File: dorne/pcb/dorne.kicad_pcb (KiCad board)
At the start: 2 copper layers, 275.5 x 105.6 mm, 92 parts, among them J1 MJ-4PP-9, J2 OLED, J3 MJ-4PP-9, J4 OLED, SW1 SW_PUSH, SW10 SW_PUSH, SW11 SW_PUSH, SW12 SW_PUSH, SW13 SW_PUSH, SW14 SW_PUSH, SW15 SW_PUSH, SW16 SW_PUSH, SW17 SW_PUSH, SW18 SW_PUSH, SW19 SW_PUSH, SW2 SW_PUSH, SW20 SW_PUSH, SW21 SW_PUSH, SW22 SW_PUSH, SW23 SW_PUSH, SW24 SW_PUSH, SW25 SW_PUSH, SW26 SW_PUSH, SW27 SW_PUSH, SW28 SW_PUSH, SW29 SW_PUSH, SW3 SW_PUSH, SW30 SW_PUSH, SW31 SW_PUSH, SW32 SW_PUSH, SW33 SW_PUSH, SW34 SW_PUSH, SW35 SW_PUSH, SW36 SW_PUSH, SW37 SW_PUSH, SW38 SW_PUSH, SW39 SW_PUSH, SW4 SW_PUSH, SW40 SW_PUSH, SW41 SW_PUSH, SW42 SW_PUSH, SW5 SW_PUSH, SW6 SW_PUSH, SW7 SW_PUSH, SW8 SW_PUSH, SW9 SW_PUSH, U1 ProMicro, U2 ProMicro

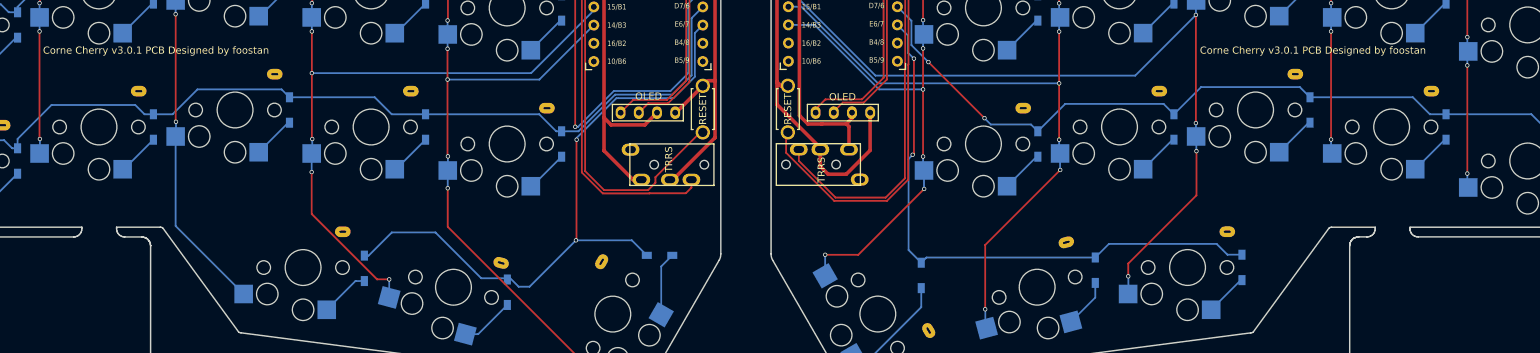
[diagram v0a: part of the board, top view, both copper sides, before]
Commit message: Fix Diode issue
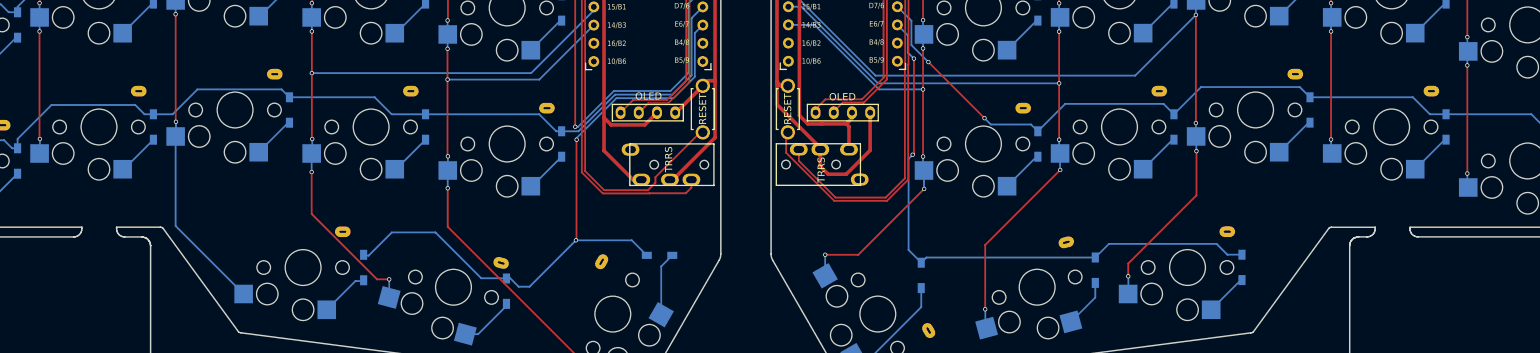
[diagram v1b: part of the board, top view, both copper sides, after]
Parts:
- U3: renamed from U1; value ProMicro -> NiceNano
- moved D19 20.4 mm to (95.1, 88.7)
- moved D20 20.1 mm to (115.0, 92.0)
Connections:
- D19 pad 2: Net-(D20-Pad2) -> Net-(D19-Pad2)
- D20 pad 2: Net-(D19-Pad2) -> Net-(D20-Pad2)
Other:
- board text removed: "Corne Cherry v3.0.1 PCB Designed by foostan"
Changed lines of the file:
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@@
     (property "Sheetname" "")
     (attr through_hole)
-    (fp_text reference "U1" (at -0.1 -0.05 270) (layer "F.SilkS") hide
+    (fp_text reference "U3" (at -0.1 -0.05 270) (layer "F.SilkS") hide
       (effects (font (size 1 1) (thickness 0.15)))
     )
-    (fp_text value "ProMicro" (at -0.45 -17) (layer "F.Fab") hide
+    (fp_text value "NiceNano" (at -0.45 -17) (layer "F.Fab") hide
       (effects (font (size 1 1) (thickness 0.15)))
     )
@@
   )
   (footprint "kbd:D3_SMD_v2" (layer "B.Cu")
-    (at 115.1325 92.105 -90)
+    (at 95.0575 88.655 -90)
     (descr "Resitance 3 pas")
     (tags "R")
@@
       (net 7 "row3") (pinfunction "K") (pintype "passive"))
     (pad "2" smd rect locked (at 1.775 0 270) (size 1.4 1) (layers "B.Cu" "B.Paste" "B.Mask")
+      (net 23 "Net-(D19-Pad2)") (pinfunction "A") (pintype "passive"))
+    (model "${KIGITHUB3D}/Diode_SMD.3dshapes/D_SOD-123.step"
+      (offset (xyz 0 0 0))
+      (scale (xyz 1 1 1))
+      (rotate (xyz 0 0 0))
+    )
+  )
+  (footprint "kbd:D3_SMD_v2" (layer "B.Cu")
+    (at 115.0075 91.955 -90)
+    (descr "Resitance 3 pas")
+    (tags "R")
+    (property "Sheetfile" "dorne.kicad_sch")
+    (property "Sheetname" "")
+    (autoplace_cost180 10)
+    (attr through_hole)
+    (fp_text reference "D20" (at 0.5 0 90) (layer "B.Fab") hide
+      (effects (font (size 0.5 0.5) (thickness 0.125)) (justify mirror))
+    )
+    (fp_text value "D" (at -0.6 0 90) (layer "B.Fab") hide
+      (effects (font (size 0.5 0.5) (thickness 0.125)) (justify mirror))
+    )
+    (fp_line (start -0.4 0) (end 0.5 0.5) (layer "B.SilkS") (width 0.15))
+    (fp_line (start -2.7 -0.75) (end 2.7 -0.75) (layer "B.SilkS") (width 0.15))
+    (fp_line (start 2.7 0.75) (end 2.7 -0.75) (layer "B.SilkS") (width 0.15))
+    (fp_line (start -0.5 0.5) (end -0.5 -0.5) (layer "B.SilkS") (width 0.15))
+    (fp_line (start -2.7 0.75) (end -2.7 -0.75) (layer "B.SilkS") (width 0.15))
+    (fp_line (start 2.7 0.75) (end -2.7 0.75) (layer "B.SilkS") (width 0.15))
+    (fp_line (start 0.5 -0.5) (end -0.4 0) (layer "B.SilkS") (width 0.15))
+    (fp_line (start 0.5 0.5) (end 0.5 -0.5) (layer "B.SilkS") (width 0.15))
+    (pad "1" smd rect locked (at -1.775 0 270) (size 1.4 1) (layers "B.Cu" "B.Paste" "B.Mask")
+      (net 7 "row3") (pinfunction "K") (pintype "passive"))
+    (pad "2" smd rect locked (at 1.775 0 270) (size 1.4 1) (layers "B.Cu" "B.Paste" "B.Mask")
       (net 24 "Net-(D20-Pad2)") (pinfunction "A") (pintype "passive"))
-    (model "${KIGITHUB3D}/Diode_SMD.3dshapes/D_SOD-123.step"
-      (offset (xyz 0 0 0))
-      (scale (xyz 1 1 1))
-      (rotate (xyz 0 0 0))
-    )
-  )
-  (footprint "kbd:D3_SMD_v2" (layer "B.Cu")
-    (at 95.1645 88.765 -90)
-    (descr "Resitance 3 pas")
-    (tags "R")
-    (property "Sheetfile" "dorne.kicad_sch")
-    (property "Sheetname" "")
-    (autoplace_cost180 10)
-    (attr through_hole)
-    (fp_text reference "D20" (at 0.5 0 90) (layer "B.Fab") hide
-      (effects (font (size 0.5 0.5) (thickness 0.125)) (justify mirror))
-    )
-    (fp_text value "D" (at -0.6 0 90) (layer "B.Fab") hide
-      (effects (font (size 0.5 0.5) (thickness 0.125)) (justify mirror))
-    )
-    (fp_line (start -0.4 0) (end 0.5 0.5) (layer "B.SilkS") (width 0.15))
-    (fp_line (start -2.7 -0.75) (end 2.7 -0.75) (layer "B.SilkS") (width 0.15))
-    (fp_line (start 2.7 0.75) (end 2.7 -0.75) (layer "B.SilkS") (width 0.15))
-    (fp_line (start -0.5 0.5) (end -0.5 -0.5) (layer "B.SilkS") (width 0.15))
-    (fp_line (start -2.7 0.75) (end -2.7 -0.75) (layer "B.SilkS") (width 0.15))
-    (fp_line (start 2.7 0.75) (end -2.7 0.75) (layer "B.SilkS") (width 0.15))
-    (fp_line (start 0.5 -0.5) (end -0.4 0) (layer "B.SilkS") (width 0.15))
-    (fp_line (start 0.5 0.5) (end 0.5 -0.5) (layer "B.SilkS") (width 0.15))
-    (pad "1" smd rect locked (at -1.775 0 270) (size 1.4 1) (layers "B.Cu" "B.Paste" "B.Mask")
-      (net 7 "row3") (pinfunction "K") (pintype "passive"))
-    (pad "2" smd rect locked (at 1.775 0 270) (size 1.4 1) (layers "B.Cu" "B.Paste" "B.Mask")
-      (net 23 "Net-(D19-Pad2)") (pinfunction "A") (pintype "passive"))
     (model "${KIGITHUB3D}/Diode_SMD.3dshapes/D_SOD-123.step"
       (offset (xyz 0 0 0))
@@
   (gr_line (start 247.204616 22.028252) (end 241.0775 22.028252) (layer "Edge.Cuts") (width 0.2))
   (gr_line (start 285.204501 83.028073) (end 279.0775 83.028073) (layer "Edge.Cuts") (width 0.2))
-  (gr_text "Corne Cherry v3.0.1 PCB Designed by foostan" (at 50.2825 58.33) (layer "F.SilkS")
-    (effects (font (size 1 1) (thickness 0.125)) (justify left))
-  )
-  (gr_text "Corne Cherry v3.0.1 PCB Designed by foostan" (at 211.8325 58.33) (layer "F.SilkS")
-    (effects (font (size 1 1) (thickness 0.125)) (justify left))
-  )
   (dimension (type aligned) (layer "Dwgs.User")
     (pts (xy 10.5845 117.784) (xy 10.5845 11.984))

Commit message: Left half is routed better now
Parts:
- U3: value NiceNano -> nice_nano; footprint kbd:ProMicro_v3 -> nicenano:nice_nano; moved to B.Cu
- moved D21 3.22 mm to (133.7, 88.8), turned to -30 degrees
- moved D20 1.31 mm to (114.8, 93.2), turned to -105 degrees
- moved D19 0.94 mm to (94.1, 88.6)
- moved U3 0.51 mm to (134.8, 45.9), turned to -90 degrees
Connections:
- U3 pad 1: LED -> unconnected-(U3-Pad1)
- U3 pad 24: unconnected-(U1-Pad24) -> BAT
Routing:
- net row0: track 138.7 -> 289.9 mm
- net (no net): track 0.00 -> 38.0 mm, vias 0 -> 4
- net SDA: track 32.4 -> 0.00 mm
- net row2: track 135.2 -> 167.6 mm
- net col0: track 159.4 -> 187.8 mm, vias 0 -> 4
- net SCL: track 27.7 -> 0.00 mm
- net col1: track 138.2 -> 165.8 mm, vias 5 -> 6
- net row3: track 89.5 -> 99.1 mm, vias 2 -> 0
- net row1: track 155.4 -> 148.0 mm, vias 2 -> 0
- net col3: track 124.8 -> 128.3 mm, vias 5 -> 7
- net col4: track 106.6 -> 110.0 mm
- net Net-(D21-Pad2): track 8.93 -> 5.76 mm
- net col2: track 118.8 -> 121.6 mm
- net Net-(D20-Pad2): track 7.55 -> 6.25 mm
- net Net-(D19-Pad2): track 6.92 -> 5.95 mm
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
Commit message: Better routing
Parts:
- moved D20 5.72 mm to (117.1, 88.0), turned to -90 degrees
- moved D21 3.00 mm to (136.6, 88.0), turned to -90 degrees
- moved D42 1.25 mm to (172.9, 88.5)
- moved D40 1.14 mm to (217.7, 87.5)
- moved D19 0.58 mm to (94.1, 88.0)
- moved D41 0.53 mm to (197.2, 88.5)
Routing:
- net row0: track 289.9 -> 161.9 mm
- net (no net): track 38.0 -> 128.0 mm, vias 4 -> 0
- net reset_r: track 85.1 -> 0.00 mm
- net SDA_r: track 32.4 -> 0.00 mm
- net row2_r: track 134.0 -> 162.9 mm, vias 2 -> 0
- net SCL_r: track 27.9 -> 0.00 mm
- net row0_r: track 143.4 -> 170.5 mm, vias 2 -> 1
- net row1_r: track 125.3 -> 151.9 mm
- net col1_r: track 137.9 -> 163.9 mm, vias 5 -> 6
- net col0_r: track 157.4 -> 181.6 mm, vias 4 -> 6
- net row2: track 167.6 -> 153.7 mm
- net Net-(D20-Pad2): track 6.25 -> 14.8 mm
- net col3_r: track 130.0 -> 124.9 mm, vias 6 -> 7
- net row3: track 99.1 -> 96.0 mm
- net GNDA: track 77.7 -> 75.6 mm
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
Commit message: Reset and power WIP
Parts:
- RSW1: moved to B.Cu
- moved RSW1 37.8 mm to (139.8, 28.8), turned to 180 degrees
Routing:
- net reset: track 59.6 -> 12.8 mm
- net GND: track 66.1 -> 70.1 mm
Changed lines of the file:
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@@
       (sketchpadsonfab false)
       (subtractmaskfromsilk false)
-      (outputformat 5)
+      (outputformat 1)
       (mirror false)
       (drillshape 0)
@@
     )
   )
-  (footprint "kbd:ResetSW_1side" (layer "F.Cu")
-    (at 142.4245 66.531 -90)
-    (property "Sheetfile" "dorne.kicad_sch")
-    (property "Sheetname" "")
-    (attr through_hole)
-    (fp_text reference "RSW1" (at 0 2.55 -90) (layer "F.SilkS") hide
-      (effects (font (size 1 1) (thickness 0.15)))
-    )
-    (fp_text value "SW_PUSH" (at 0 -2.55 -90) (layer "F.Fab")
-      (effects (font (size 1 1) (thickness 0.15)))
-    )
-    (fp_text user "RESET" (at 0 0 -90) (layer "F.SilkS")
-      (effects (font (size 1 1) (thickness 0.15)))
-    )
-    (fp_line (start 2.85 1.6) (end 2.85 1.35) (layer "F.SilkS") (width 0.15))
-    (fp_line (start -2.85 1.6) (end -2.85 1.35) (layer "F.SilkS") (width 0.15))
-    (fp_line (start -2.85 -1.6) (end 2.85 -1.6) (layer "F.SilkS") (width 0.15))
-    (fp_line (start -2.85 1.6) (end 2.85 1.6) (layer "F.SilkS") (width 0.15))
-    (fp_line (start -2.85 -1.6) (end -2.85 -1.35) (layer "F.SilkS") (width 0.15))
-    (fp_line (start 2.85 -1.6) (end 2.85 -1.35) (layer "F.SilkS") (width 0.15))
-    (pad "1" thru_hole circle locked (at 3.25 0 270) (size 2 2) (drill 1.3) (layers *.Cu "B.Mask")
-      (net 35 "reset") (pinfunction "1") (pintype "passive"))
-    (pad "2" thru_hole circle locked (at -3.25 0 270) (size 2 2) (drill 1.3) (layers *.Cu "B.Mask")
-      (net 26 "GND") (pinfunction "2") (pintype "passive"))
-    (model "/Users/foostan/src/github.com/foostan/kbd/kicad-packages3D/kbd.3dshapes/tact-switch.step"
-      (offset (xyz 0 0 3.47))
-      (scale (xyz 1 1 1))
-      (rotate (xyz 0 0 0))
-    )
-  )
   (footprint "kbd:ChocV1_V2_Hotswap" (layer "F.Cu")
     (at 39.1075 35.78)
@@
     )
   )
+  (footprint "kbd:ResetSW_1side" (layer "B.Cu")
+    (at 139.8325 28.84 180)
+    (property "Sheetfile" "dorne.kicad_sch")
+    (property "Sheetname" "")
+    (attr through_hole)
+    (fp_text reference "RSW1" (at 0 -2.55) (layer "B.SilkS") hide
+      (effects (font (size 1 1) (thickness 0.15)) (justify mirror))
+    )
+    (fp_text value "SW_PUSH" (at 0 2.55) (layer "B.Fab")
+      (effects (font (size 1 1) (thickness 0.15)) (justify mirror))
+    )
+    (fp_text user "RESET" (at 0 0) (layer "B.SilkS")
+      (effects (font (size 1 1) (thickness 0.15)) (justify mirror))
+    )
+    (fp_line (start 2.85 -1.6) (end 2.85 -1.35) (layer "B.SilkS") (width 0.15))
+    (fp_line (start -2.85 -1.6) (end -2.85 -1.35) (layer "B.SilkS") (width 0.15))
+    (fp_line (start -2.85 1.6) (end 2.85 1.6) (layer "B.SilkS") (width 0.15))
+    (fp_line (start -2.85 -1.6) (end 2.85 -1.6) (layer "B.SilkS") (width 0.15))
+    (fp_line (start -2.85 1.6) (end -2.85 1.35) (layer "B.SilkS") (width 0.15))
+    (fp_line (start 2.85 1.6) (end 2.85 1.35) (layer "B.SilkS") (width 0.15))
+    (pad "1" thru_hole circle locked (at 3.25 0 180) (size 2 2) (drill 1.3) (layers *.Cu "F.Mask")
+      (net 35 "reset") (pinfunction "1") (pintype "passive"))
+    (pad "2" thru_hole circle locked (at -3.25 0 180) (size 2 2) (drill 1.3) (layers *.Cu "F.Mask")
+      (net 26 "GND") (pinfunction "2") (pintype "passive"))
+    (model "/Users/foostan/src/github.com/foostan/kbd/kicad-packages3D/kbd.3dshapes/tact-switch.step"
+      (offset (xyz 0 0 3.47))
+      (scale (xyz 1 1 1))
+      (rotate (xyz 0 0 0))
+    )
+  )
   (footprint "kbd:D3_SMD_v2" (layer "B.Cu")
     (at 27.7345 35.776875 -90)
@@
   (segment (start 144.1345 62.571) (end 144.1345 70.514) (width 0.508) (layer "F.Cu") (net 26))
   (segment (start 142.4239 37.022) (end 142.4239 39.562) (width 0.508) (layer "F.Cu") (net 26))
-  (segment (start 142.4245 63.281) (end 138.6775 67.028) (width 0.508) (layer "F.Cu") (net 26))
   (segment (start 142.4239 39.562) (end 144.1345 41.2726) (width 0.508) (layer "F.Cu") (net 26))
   (segment (start 144.1345 62.571) (end 143.1345 62.571) (width 0.508) (layer "F.Cu") (net 26))
@@
   (segment (start 144.1345 41.2726) (end 144.1345 62.571) (width 0.508) (layer "F.Cu") (net 26))
   (segment (start 144.1345 70.514) (end 138.2565 76.392) (width 0.508) (layer "F.Cu") (net 26))
+  (segment (start 142.4325 37.02) (end 144.153234 35.299266) (width 0.25) (layer "B.Cu") (net 26))
+  (segment (start 144.153234 29.910734) (end 143.0825 28.84) (width 0.25) (layer "B.Cu") (net 26))
+  (segment (start 144.153234 35.299266) (end 144.153234 29.910734) (width 0.25) (layer "B.Cu") (net 26))
   (segment (start 128.468501 40.778001) (end 128.6275 40.937) (width 0.508) (layer "F.Cu") (net 27))
   (segment (start 129.6205 68.73) (end 134.3265 68.73) (width 0.508) (layer "F.Cu") (net 27))
@@
   (segment (start 142.4239 34.482) (end 141.1559 33.214) (width 0.254) (layer "F.Cu") (net 34))
   (segment (start 125.534502 41.255972) (end 125.534502 75.370986) (width 0.254) (layer "F.Cu") (net 34))
-  (segment (start 127.2039 37.022) (end 126.038522 38.187378) (width 0.254) (layer "F.Cu") (net 35))
-  (segment (start 125.988513 41.444029) (end 125.988513 75.182929) (width 0.254) (layer "F.Cu") (net 35))
-  (segment (start 125.988513 75.182929) (end 128.645584 77.84) (width 0.254) (layer "F.Cu") (net 35))
-  (segment (start 135.8075 76.819968) (end 135.8075 76.04) (width 0.254) (layer "F.Cu") (net 35))
-  (segment (start 128.645584 77.84) (end 134.787468 77.84) (width 0.254) (layer "F.Cu") (net 35))
-  (segment (start 126.038522 41.39402) (end 125.988513 41.444029) (width 0.254) (layer "F.Cu") (net 35))
-  (segment (start 126.038522 38.187378) (end 126.038522 41.39402) (width 0.254) (layer "F.Cu") (net 35))
-  (segment (start 135.8075 76.04) (end 142.0665 69.781) (width 0.254) (layer "F.Cu") (net 35))
-  (segment (start 134.787468 77.84) (end 135.8075 76.819968) (width 0.254) (layer "F.Cu") (net 35))
+  (segment (start 135.3725 28.84) (end 136.5825 28.84) (width 0.25) (layer "B.Cu") (net 35))
+  (segment (start 127.1925 37.02) (end 135.3725 28.84) (width 0.25) (layer "B.Cu") (net 35))
   (segment (start 280.2375 41.675) (end 284.2325 37.68) (width 0.25) (layer "B.Cu") (net 40))
   (segment (start 167.3525 43.3) (end 167.3525 44.9056) (width 0.25) (layer "F.Cu") (net 41))

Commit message: Saving state
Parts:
- removed J3: MJ-4PP-9, kbd:MJ-4PP-9_1side
- removed J4: OLED, kbd:OLED_1side
- removed U2: ProMicro, kbd:ProMicro_v3
- added H0: MountingHole_Pad, Connector_Pin:Pin_D1.0mm_L10.0mm, F.Cu at (132.3, 37.0)
- added H1: MountingHole_Pad, Connector_Pin:Pin_D1.0mm_L10.0mm, F.Cu at (137.4, 37.0)
- added SW0: SW_SPDT, lib:ALPS-SSSS811101-0, B.Cu at (134.9, 28.8)
- added U4: nice_nano, nicenano:nice_nano, B.Cu at (162.0, 45.9)
- J2: value OLED -> MJ-4PP-9; footprint kbd:OLED_1side -> kbd:MJ-4PP-9_1side
- RSW1: footprint kbd:ResetSW_1side -> Button_Switch_SMD:SW_Push_SPST_NO_Alps_SKRK; moved to F.Cu
- RSW2: footprint kbd:ResetSW_1side -> Button_Switch_SMD:SW_Push_SPST_NO_Alps_SKRK
- moved RSW1 37.4 mm to (134.8, 65.9), turned to 0 degrees
- moved J2 23.0 mm to (152.8, 74.3), turned to 90 degrees
- moved RSW2 7.82 mm to (162.1, 65.9), turned to 0 degrees
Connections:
- U3 pad 24: BAT -> bat_in
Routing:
- net (no net): track 128.0 -> 0.00 mm
- net col5_r: track 84.8 -> 0.00 mm, vias 7 -> 4
- net col4_r: track 110.6 -> 195.4 mm, vias 7 -> 10
- net GNDA: track 75.6 -> 27.4 mm
- net reset: track 12.8 -> 32.9 mm
- net VCC: track 48.8 -> 40.3 mm
- net bat_pos: track 0.00 -> 7.16 mm
- net bat_in: track 0.00 -> 5.75 mm
- net VDD: track 41.2 -> 37.1 mm
- net GND: track 70.1 -> 66.1 mm
- net Net-(D20-Pad2): track 14.8 -> 12.7 mm
- net row1_r: track 151.9 -> 151.0 mm
- net Net-(D19-Pad2): track 6.53 -> 5.96 mm
- net Net-(D40-Pad2): track 7.58 -> 7.06 mm

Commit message: Finished everything??
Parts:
- removed SW0: SW_SPDT, lib:ALPS-SSSS811101-0
- added H2: MountingHole_Pad, Connector_Pin:Pin_D1.0mm_L10.0mm, F.Cu at (160.6, 37.0)
- added H3: MountingHole_Pad, Connector_Pin:Pin_D1.0mm_L10.0mm, F.Cu at (164.6, 37.0)
- added PSW0: SW_SPDT, lib:ALPS-SSSS811101-0, B.Cu at (134.9, 28.8)
- added PSW1: SW_SPDT, lib:ALPS-SSSS811101-0, B.Cu at (162.1, 28.9)
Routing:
- net col5_r: track 0.00 -> 84.8 mm, vias 4 -> 7
- net col4_r: track 195.4 -> 112.2 mm, vias 10 -> 7
- net GNDA: track 27.4 -> 79.3 mm
- net reset_r: track 0.00 -> 32.8 mm
- net VDD: track 37.1 -> 47.7 mm, vias 0 -> 2
- net bat_pos_r: track 0.00 -> 6.64 mm
- net bat_in_r: track 0.00 -> 5.73 mm
- net row3_r: track 81.3 -> 86.3 mm, vias 2 -> 0
- net VCC: track 40.3 -> 45.2 mm
- net row2_r: track 162.8 -> 159.5 mm
- net data_r: track 61.7 -> 63.5 mm
- net col0_r: track 181.6 -> 179.9 mm

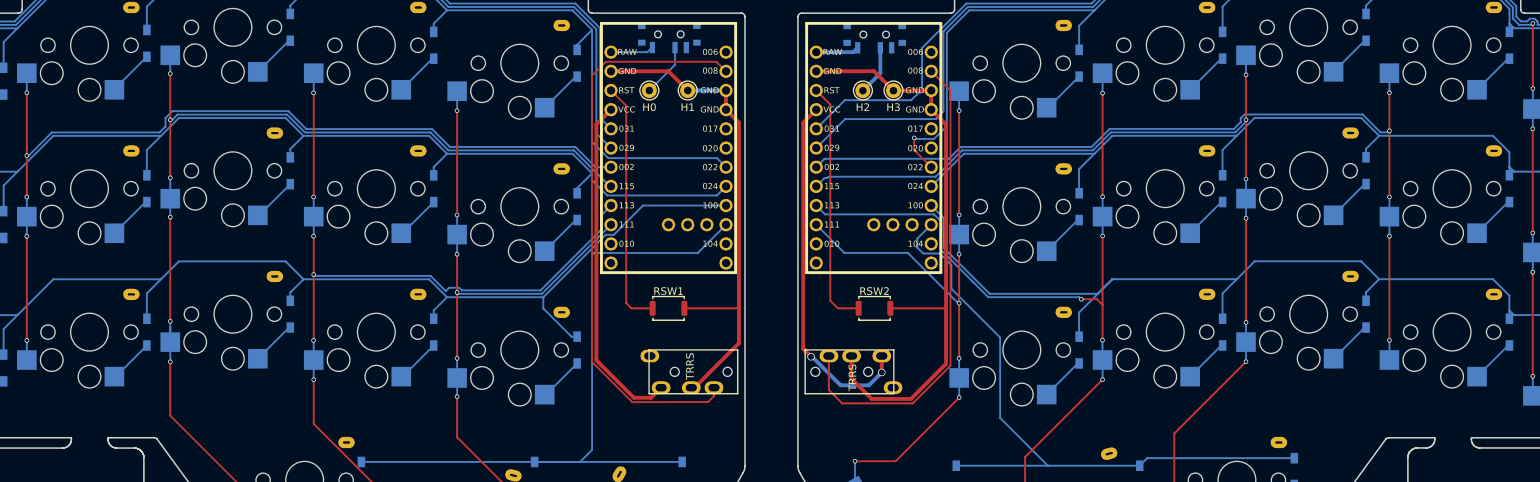
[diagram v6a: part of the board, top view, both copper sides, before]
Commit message: Trying to fix the edge cuts and add back in the M2 holes
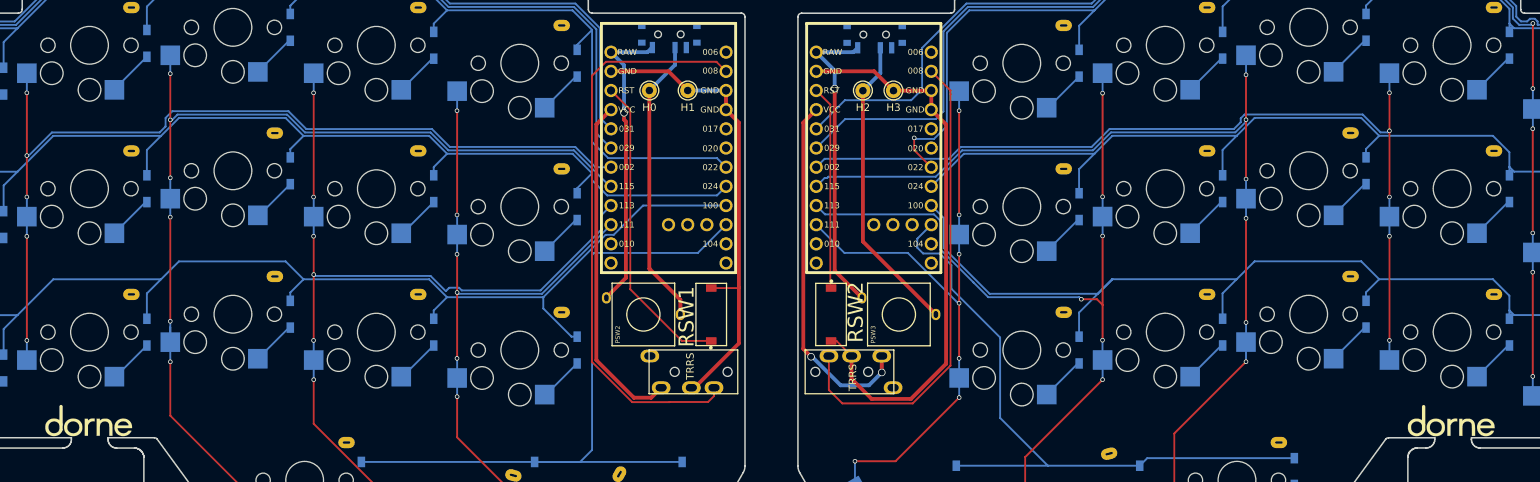
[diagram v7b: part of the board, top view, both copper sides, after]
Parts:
- added G***: LOGO, lib:dorne-logo-horizontal, F.Cu at (58.1, 81.7)
- added G***: LOGO, lib:dorne-logo-horizontal, F.Cu at (238.6, 81.7)
- added G***: LOGO, lib:dorne-logo-horizontal, B.Cu at (58.1, 81.7)
- added G***: LOGO, lib:dorne-logo-horizontal, B.Cu at (238.6, 81.7)
- added PSW2: SW_SPST, buttons:SW_L068-A, F.Cu at (131.5, 66.7)
- added PSW3: SW_SPST, buttons:SW_L068-A, F.Cu at (165.3, 66.7)
- RSW1, RSW2: footprint Button_Switch_SMD:SW_Push_SPST_NO_Alps_SKRK -> lib:CK_Components-KSR223GNCLFG-0
- moved RSW2 5.82 mm to (156.3, 66.7), turned to -90 degrees
- moved RSW1 5.72 mm to (140.5, 66.7), turned to 90 degrees
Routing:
- net bat_in_r: track 5.73 -> 40.8 mm, vias 0 -> 1
- net bat_in: track 5.75 -> 40.1 mm, vias 0 -> 1
- net bat_pos_r: track 6.64 -> 40.3 mm
- net bat_pos: track 7.16 -> 38.5 mm
- net reset: track 32.8 -> 40.9 mm
- net reset_r: track 32.8 -> 26.7 mm
- net GNDA: track 79.3 -> 75.4 mm
- net GND: track 66.1 -> 62.5 mm
